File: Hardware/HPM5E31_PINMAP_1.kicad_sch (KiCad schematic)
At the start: 3 parts

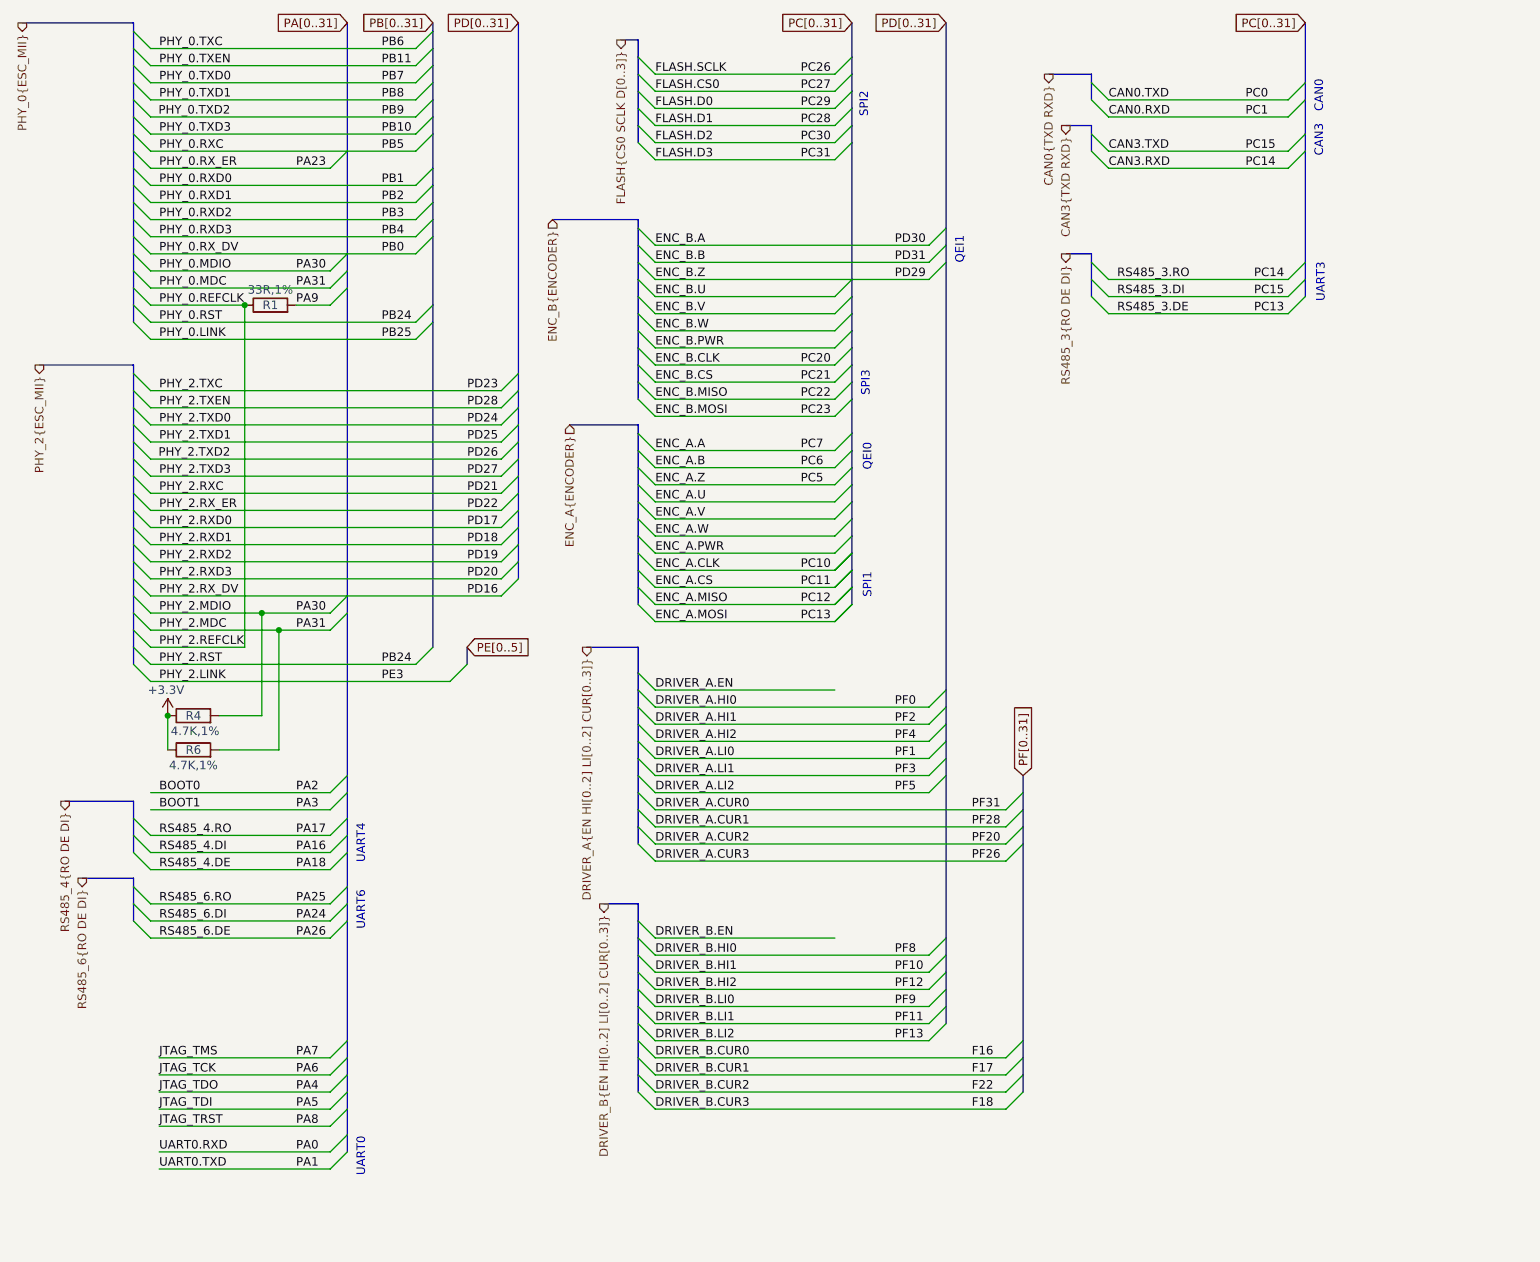
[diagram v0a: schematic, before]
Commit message: 调整引脚，拉线
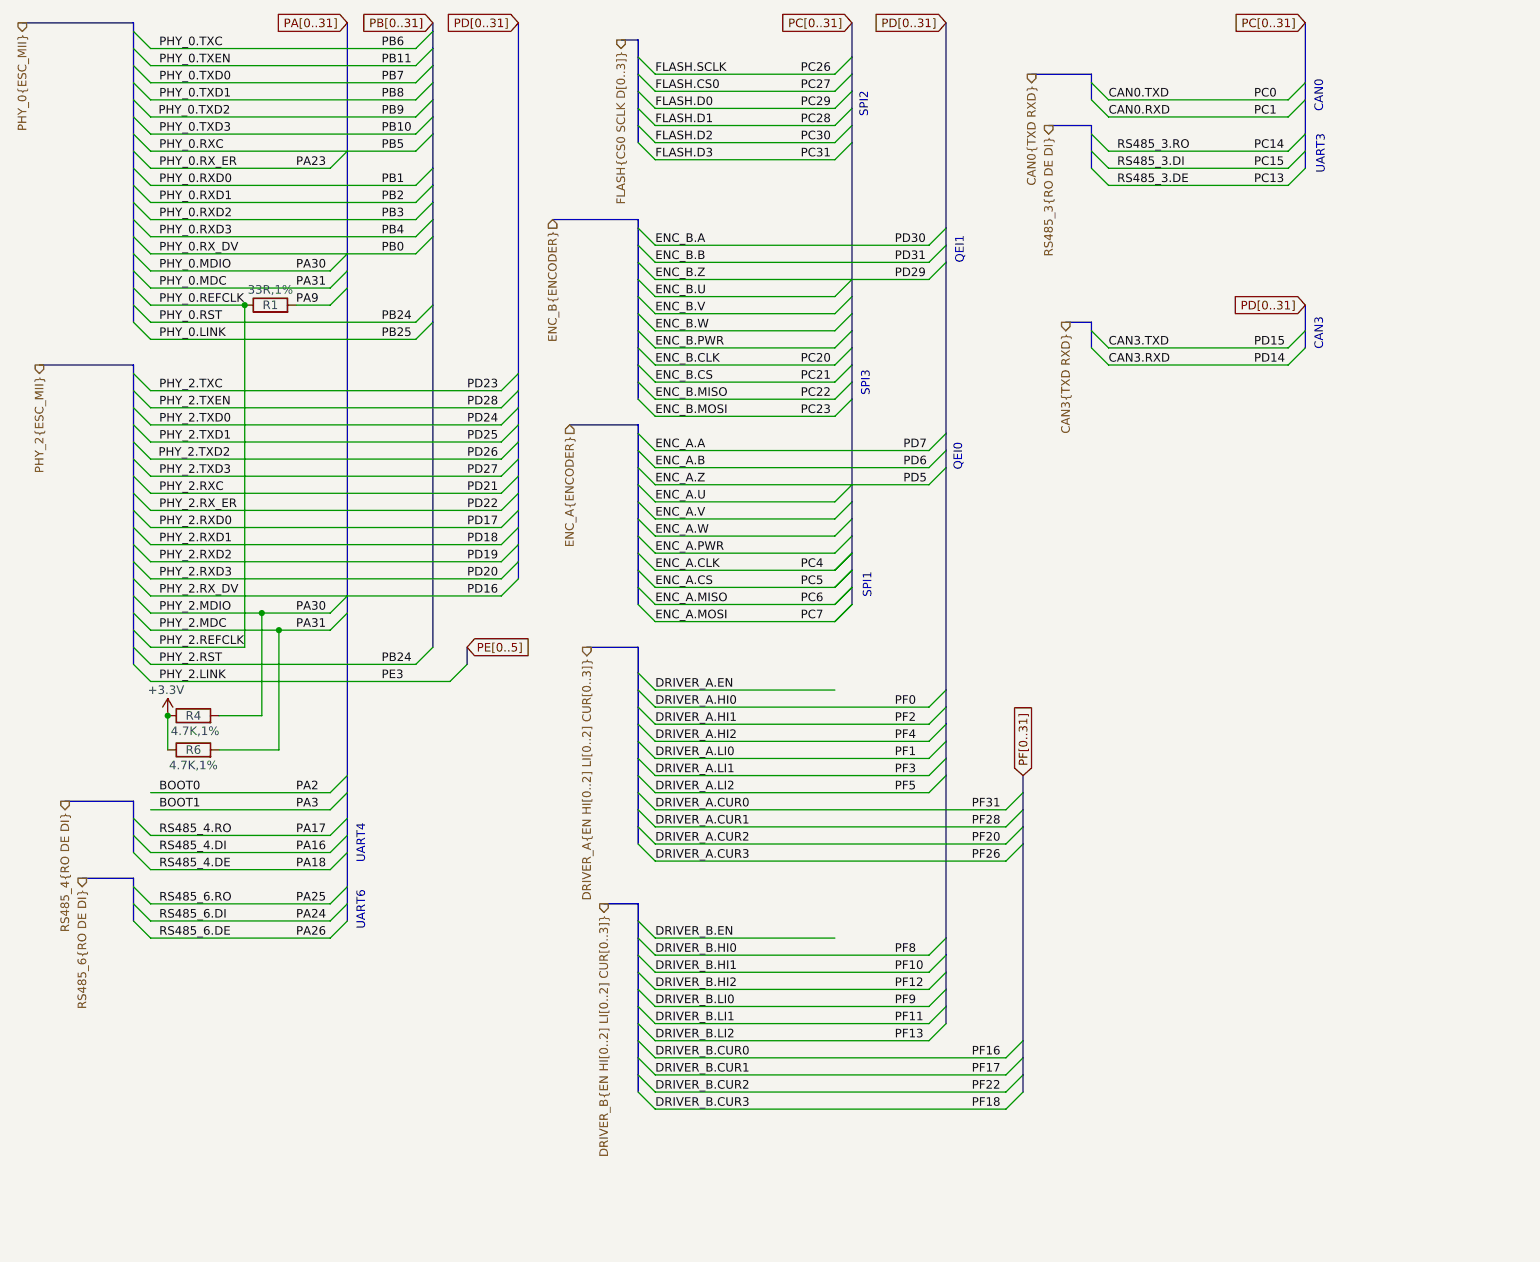
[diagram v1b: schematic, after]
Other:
- note removed: "UART0"

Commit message: 修存档拉线
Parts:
- renumbered R4 to R10, R6 to R11, R1 to R9
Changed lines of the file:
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@@
 		(on_board yes)
 		(dnp no)
-		(property "Reference" "#PWR06"
+		(property "Reference" "#PWR019"
 			(at 45.72 127 0)
 			(effects
@@
 		)
 		(pin "1"
+		)
+		(instances
+			(project "HPM5E31_ECatDualFOC"
+				(path "/a07e9810-3899-4327-ba8f-f24142a7c70e/b9a8d5a3-7d25-4818-87f6-adc719379948/6734c7c5-c927-492b-a5ca-68015457caeb"
+					(reference "#PWR019")
+					(unit 1)
+				)
+			)
 		)
 	)
@@
 		(on_board yes)
 		(dnp no)
-		(property "Reference" "R6"
+		(property "Reference" "R11"
 			(at 49.53 128.27 0)
 			(effects
@@
 		)
 		(pin "2"
+		)
+		(instances
+			(project "HPM5E31_ECatDualFOC"
+				(path "/a07e9810-3899-4327-ba8f-f24142a7c70e/b9a8d5a3-7d25-4818-87f6-adc719379948/6734c7c5-c927-492b-a5ca-68015457caeb"
+					(reference "R11")
+					(unit 1)
+				)
+			)
 		)
 	)
@@
 		(on_board yes)
 		(dnp no)
-		(property "Reference" "R4"
+		(property "Reference" "R10"
 			(at 49.53 123.19 0)
 			(effects
@@
 		)
 		(pin "2"
+		)
+		(instances
+			(project "HPM5E31_ECatDualFOC"
+				(path "/a07e9810-3899-4327-ba8f-f24142a7c70e/b9a8d5a3-7d25-4818-87f6-adc719379948/6734c7c5-c927-492b-a5ca-68015457caeb"
+					(reference "R10")
+					(unit 1)
+				)
+			)
 		)
 	)
@@
 		(on_board yes)
 		(dnp no)
-		(property "Reference" "R1"
+		(property "Reference" "R9"
 			(at 60.96 62.23 0)
 			(effects
@@
 		(pin "2"
 		)
+		(instances
+			(project "HPM5E31_ECatDualFOC"
+				(path "/a07e9810-3899-4327-ba8f-f24142a7c70e/b9a8d5a3-7d25-4818-87f6-adc719379948/6734c7c5-c927-492b-a5ca-68015457caeb"
+					(reference "R9")
+					(unit 1)
+				)
+			)
+		)
 	)

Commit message: 拉线
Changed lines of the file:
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@@
 		)
 	)
-	(label "PE2"
+	(label "PE0"
 		(at 139.7 156.21 0)
 		(effects

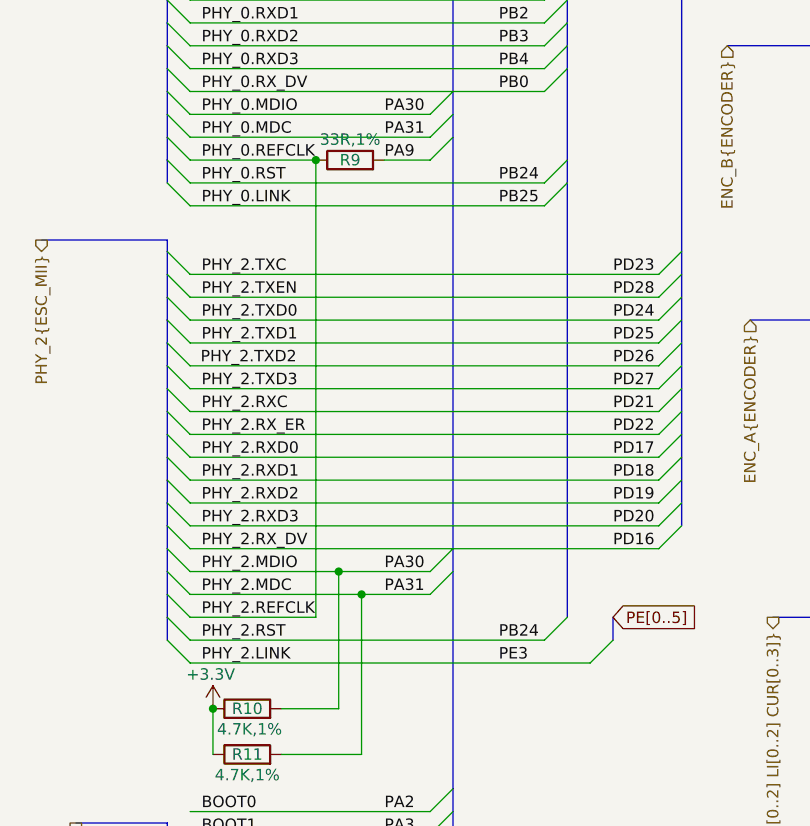
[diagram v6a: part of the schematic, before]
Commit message: 修改PCB，上传py32抱闸驱动代码，上传HPM board
调整抱闸驱动栅极电阻
急停光耦增加上拉电阻和滤波电路
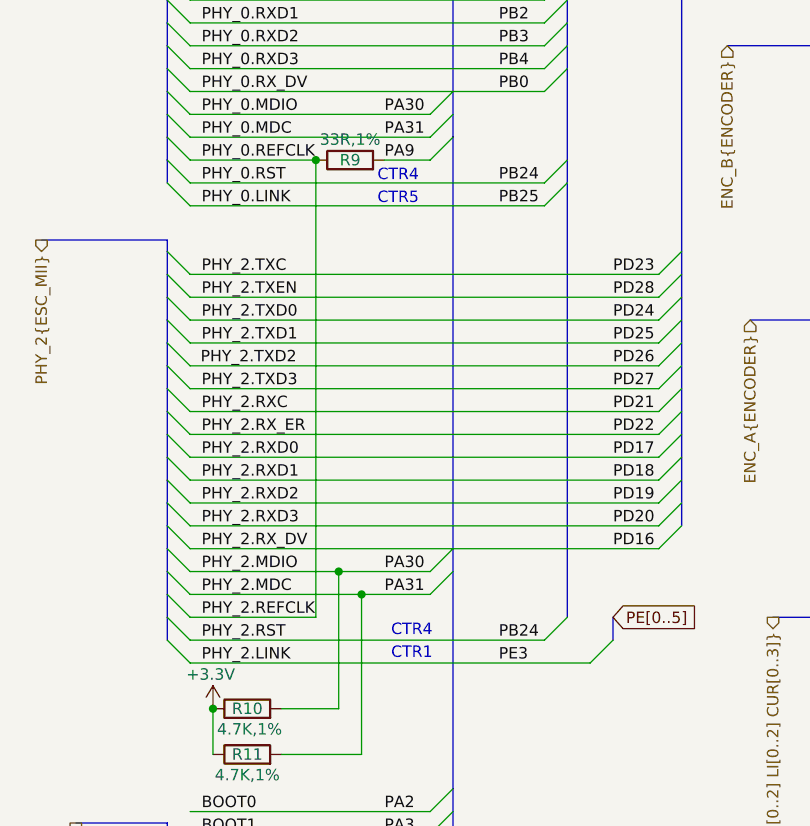
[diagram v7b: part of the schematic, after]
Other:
- note added: "CTR1"
- note added: "CTR4"
- note added: "CTR5"
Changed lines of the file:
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@@
+		)
+	)
+	(text "CTR4"
+		(exclude_from_sim no)
+		(at 67.818 114.554 0)
+		(effects
+			(font
+				(size 1.27 1.27)
+			)
+		)
+	)
+	(text "CTR5"
+		(exclude_from_sim no)
+		(at 66.294 66.548 0)
+		(effects
+			(font
+				(size 1.27 1.27)
+			)
 		)
 	)
@@
 		)
 	)
+	(text "CTR1"
+		(exclude_from_sim no)
+		(at 67.818 117.094 0)
+		(effects
+			(font
+				(size 1.27 1.27)
+			)
+		)
+	)
 	(text "QEI0"
 		(exclude_from_sim no)
@@
 		(effects
 			(font
+				(size 1.27 1.27)
+			)
+		)
+	)
+	(text "CTR4"
+		(exclude_from_sim no)
+		(at 66.294 64.008 0)
+		(effects
+			(font

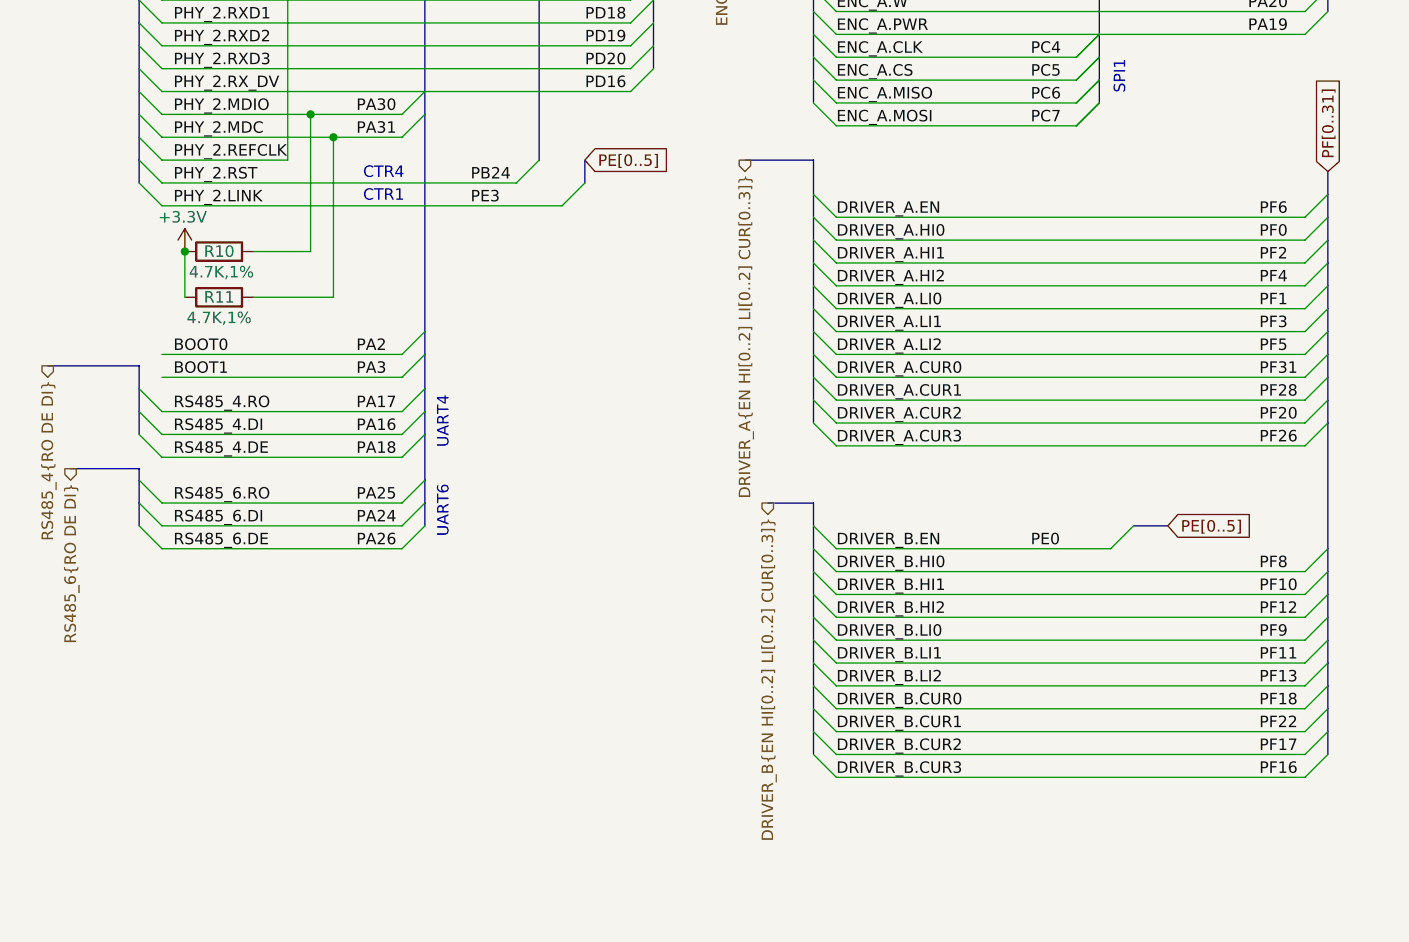
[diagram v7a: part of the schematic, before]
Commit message: PCB和foc_demo
PCB：
部分信号增加测试点
半桥增加栅极电容和RC吸收（待定），泄放mos是否需要栅极电容待测
软件：
增加foc_demo半成品
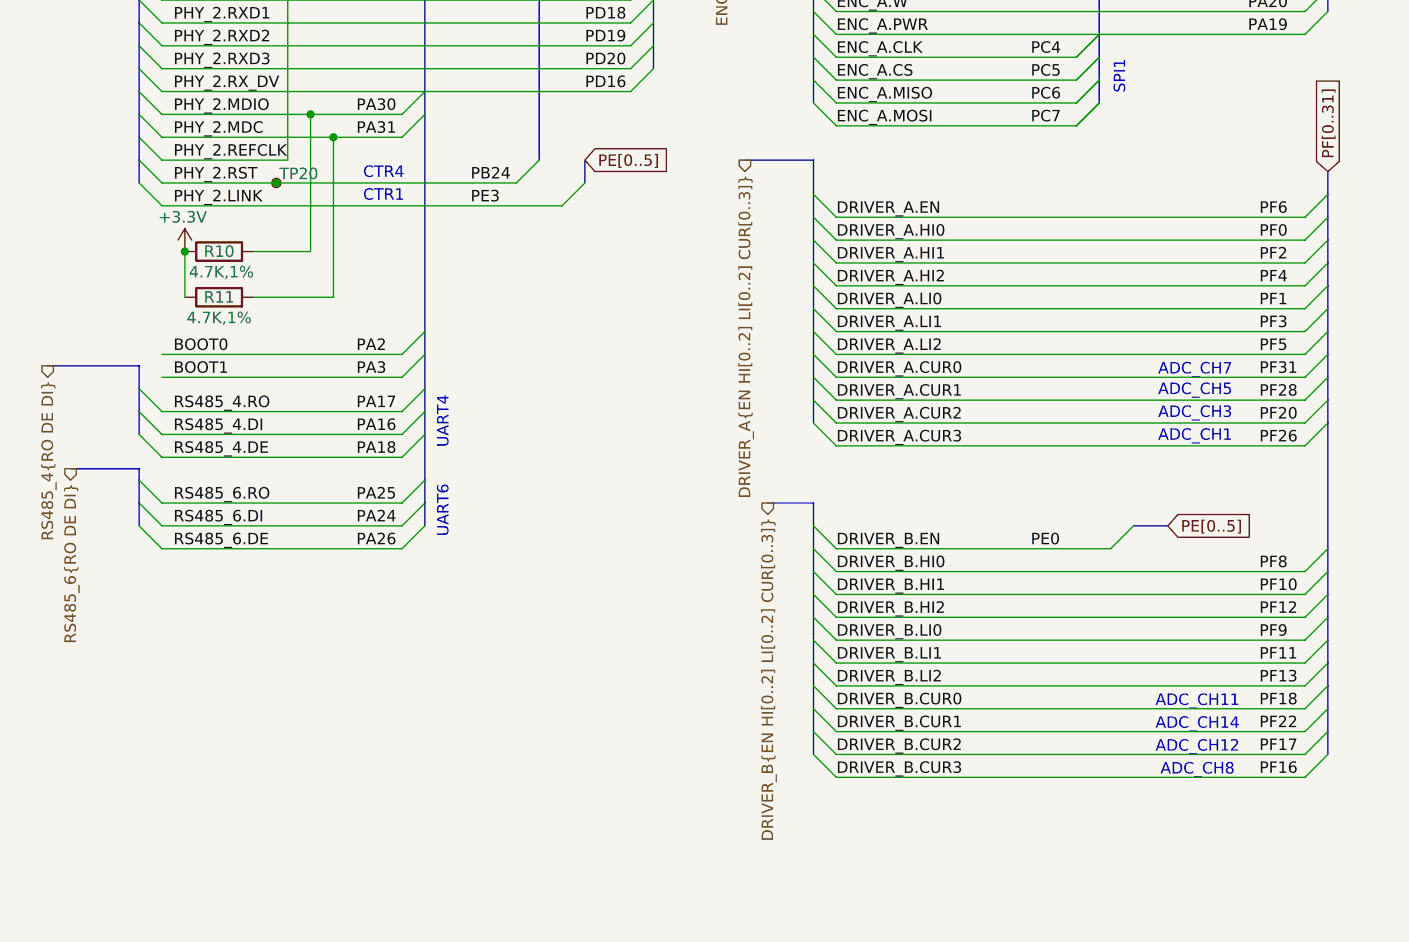
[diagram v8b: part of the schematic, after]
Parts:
- added TP20: ~, Library:test_point_0.5mm, symbol HPM6280Foc:test_point
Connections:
- net PB24: now also TP20.1
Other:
- note added: "ADC_CH1"
- note added: "ADC_CH11"
- note added: "ADC_CH12"
- note added: "ADC_CH14"
- note added: "ADC_CH3"
- note added: "ADC_CH5"
- note added: "ADC_CH7"
- note added: "ADC_CH8"
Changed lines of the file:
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@@
 		)
 	)
+	(text "ADC_CH5"
+		(exclude_from_sim no)
+		(at 157.988 138.684 0)
+		(effects
+			(font
+				(size 1.27 1.27)
+			)
+		)
+	)
+	(text "ADC_CH12"
+		(exclude_from_sim no)
+		(at 158.242 178.308 0)
+		(effects
+			(font
+				(size 1.27 1.27)
+			)
+		)
+	)
 	(text "SPI2"
 		(exclude_from_sim no)
@@
 		)
 	)
+	(text "ADC_CH14"
+		(exclude_from_sim no)
+		(at 158.242 175.768 0)
+		(effects
+			(font
+				(size 1.27 1.27)
+			)
+		)
+	)
 	(text "CTR5"
 		(exclude_from_sim no)
@@
 		)
 	)
+	(text "ADC_CH3"
+		(exclude_from_sim no)
+		(at 157.988 141.224 0)
+		(effects
+			(font
+				(size 1.27 1.27)
+			)
+		)
+	)
 	(text "UART6"
 		(exclude_from_sim no)
@@
 		)
 	)
+	(text "ADC_CH7"
+		(exclude_from_sim no)
+		(at 157.988 136.398 0)
+		(effects
+			(font
+				(size 1.27 1.27)
+			)
+		)
+	)
 	(text "QEI1"
 		(exclude_from_sim no)
@@
 		)
 	)
+	(text "ADC_CH1"
+		(exclude_from_sim no)
+		(at 157.988 143.764 0)
+		(effects
+			(font
+				(size 1.27 1.27)
+			)
+		)
+	)
 	(text "CTR1"
 		(exclude_from_sim no)
@@
 		)
 	)
+	(text "ADC_CH11"
+		(exclude_from_sim no)
+		(at 158.242 173.228 0)
+		(effects
+			(font
+				(size 1.27 1.27)
+			)
+		)
+	)
 	(text "QEI0"
 		(exclude_from_sim no)
@@
 		)
 	)
+	(text "ADC_CH8"
+		(exclude_from_sim no)
+		(at 158.242 180.848 0)
+		(effects
+			(font
+				(size 1.27 1.27)
+			)
+		)
+	)
 	(text "SPI3"
 		(exclude_from_sim no)
@@
 	)
 	(junction
+		(at 55.88 115.57)
+		(diameter 0)
+		(color 0 0 0 0)
+	)
+	(junction
 		(at 59.69 107.95)
 		(diameter 0)
@@
 	(wire
 		(pts
-			(xy 43.18 115.57) (xy 82.55 115.57)
+			(xy 43.18 115.57) (xy 55.88 115.57)
 		)
 		(stroke
@@
 	(wire
 		(pts
+			(xy 55.88 115.57) (xy 82.55 115.57)
+		)
+		(stroke
+			(width 0)
+			(type default)
+		)
+	)
+	(wire
+		(pts
 			(xy 118.11 30.48) (xy 144.78 30.48)
 		)
@@
 					(unit 1)
 				)
+			)
+		)
+	)
+	(symbol
+		(lib_id "HPM6280Foc:test_point")
+		(at 55.88 115.57 0)
+		(unit 1)
+		(exclude_from_sim no)
+		(in_bom yes)
+		(on_board yes)
+		(dnp no)
+		(property "Reference" "TP20"
+			(at 58.3902 114.554 0)
+			(effects
+				(font
+					(size 1.27 1.27)
+				)
+			)
+		)
+		(property "Value" "~"
+			(at 55.88 115.57 0)
+			(effects
+				(font
+					(size 1.27 1.27)
+				)
+				(hide yes)
+			)
+		)
+		(property "Footprint" "Library:test_point_0.5mm"
+			(at 55.88 115.57 0)
+			(effects
+				(font
+					(size 1.27 1.27)
+				)
+				(hide yes)
+			)
+		)
+		(property "Datasheet" ""
+			(at 55.88 115.57 0)
+			(effects
+				(font
+					(size 1.27 1.27)
+				)
+				(hide yes)
+			)
+		)
+		(property "Description" ""
+			(at 55.88 115.57 0)
+			(effects
+				(font
+					(size 1.27 1.27)
+				)
+				(hide yes)
+			)
+		)
+		(pin "1"
+		)
+		(instances
+			(project "HPM5E31_ECatDualFOC"
+				(path "/a07e9810-3899-4327-ba8f-f24142a7c70e/b9a8d5a3-7d25-4818-87f6-adc719379948/6734c7c5-c927-492b-a5ca-68015457caeb"
+					(reference "TP20")
+					(unit 1)
+				)
